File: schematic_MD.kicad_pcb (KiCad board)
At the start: 2 copper layers, 100 x 100 mm, 101 parts, among them J1 XT60, J10 Gate_PWR_Jump, J13 EXPWR_GND, J2 XT60, J3 XT60, J4 CAN_Bus, J5 Rotaly_encoder_1, J6 Rotaly_encoder_2, J7 Z_jumper, J8 Z_jumper, J9 Conn_02x01, Q1 SQJ886EP-T1_GE3, Q2 SQJ886EP-T1_GE3, Q3 SQJ886EP-T1_GE3, Q4 SQJ886EP-T1_GE3, Q5 SQJ886EP-T1_GE3, Q6 SQJ886EP-T1_GE3, Q7 SQJ886EP-T1_GE3, Q8 SQJ886EP-T1_GE3, SW1 SW_MEC_5G, U2 XC6206P332MR-G, U6 STM32F405RGTx, U7 MAX3051, U8 L78M05ABDT-TR

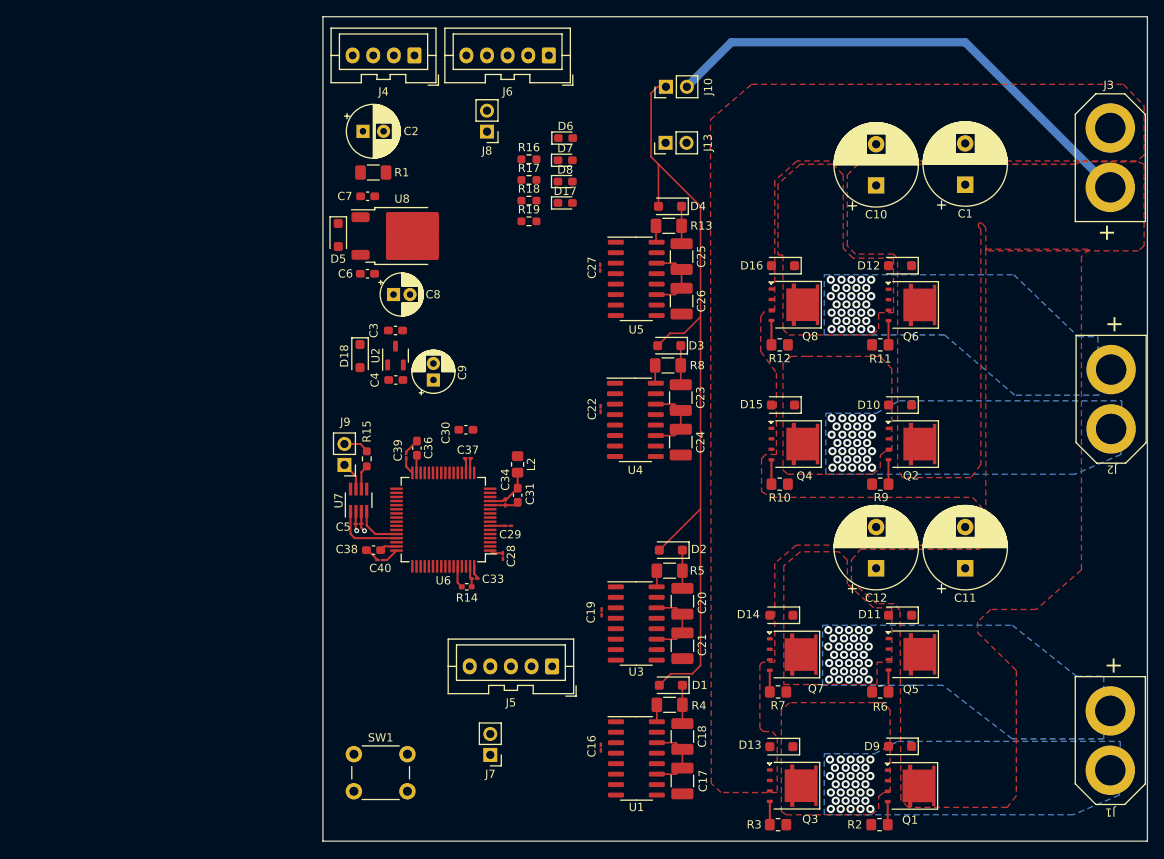
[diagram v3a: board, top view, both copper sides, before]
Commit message: Change gate driver
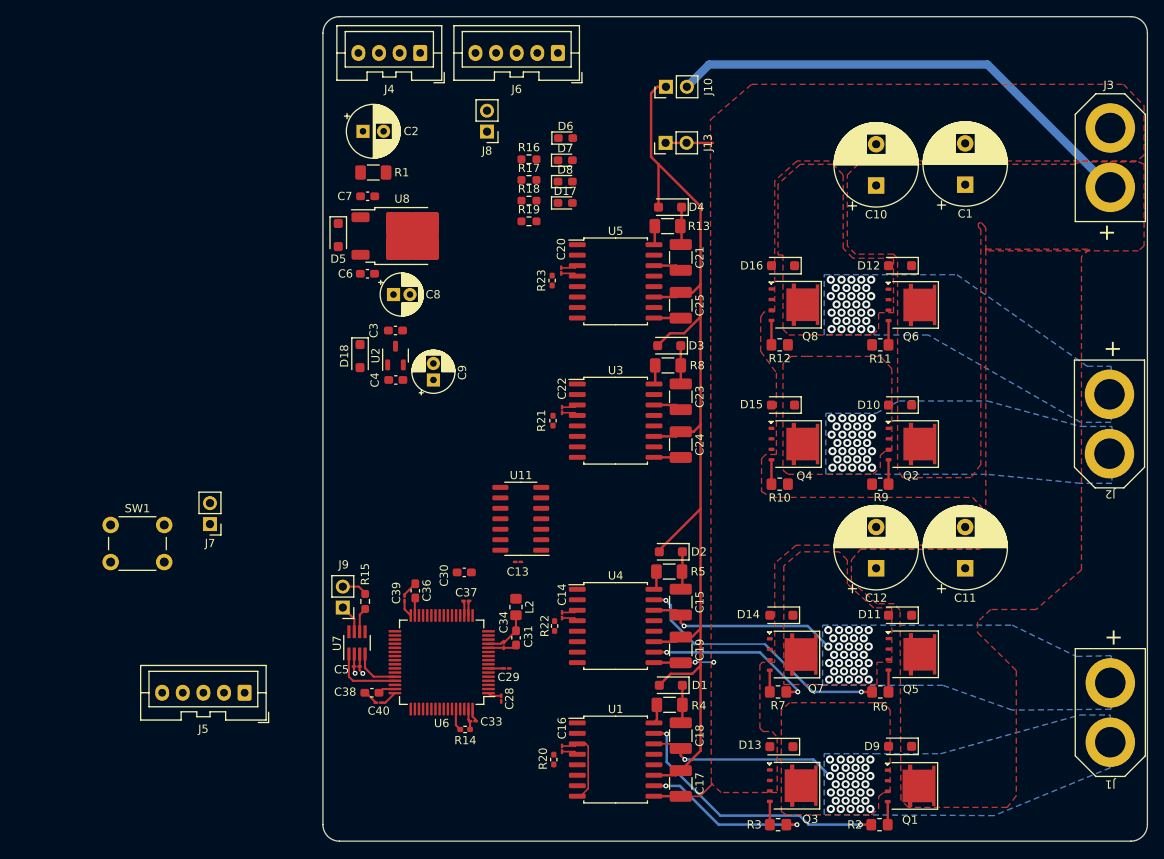
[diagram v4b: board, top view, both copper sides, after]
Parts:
- removed C26: 10u, Capacitor_SMD:C_1210_3225Metric_Pad1.33x2.70mm_HandSolder
- removed C27: 0.1u, Capacitor_SMD:C_01005_0402Metric_Pad0.57x0.30mm_HandSolder
- added C13: 0.1u, Capacitor_SMD:C_01005_0402Metric_Pad0.57x0.30mm_HandSolder, F.Cu at (118.7, 106.1)
- added C14: 0.1u, Capacitor_SMD:C_01005_0402Metric_Pad0.57x0.30mm_HandSolder, F.Cu at (124.0, 112.6)
- added C15: 10u, Capacitor_SMD:C_1210_3225Metric_Pad1.33x2.70mm_HandSolder, F.Cu at (138.4, 111.0)
- added R20: 10k, Resistor_SMD:R_0402_1005Metric_Pad0.72x0.64mm_HandSolder, F.Cu at (123.0, 130.1)
- added R21: 10k, Resistor_SMD:R_0402_1005Metric_Pad0.72x0.64mm_HandSolder, F.Cu at (122.9, 89.0)
- added R22: 10k, Resistor_SMD:R_0402_1005Metric_Pad0.72x0.64mm_HandSolder, F.Cu at (123.1, 113.9)
- added R23: 10k, Resistor_SMD:R_0402_1005Metric_Pad0.72x0.64mm_HandSolder, F.Cu at (122.8, 72.0)
- added U11: 74HC04, Package_SO:SOIC-14_3.9x8.7mm_P1.27mm, F.Cu at (119.0, 100.9)
- C19: value 0.1u -> 10u; footprint Capacitor_SMD:C_01005_0402Metric_Pad0.57x0.30mm_HandSolder -> Capacitor_SMD:C_1210_3225Metric_Pad1.33x2.70mm_HandSolder
- C20: value 10u -> 0.1u; footprint Capacitor_SMD:C_1210_3225Metric_Pad1.33x2.70mm_HandSolder -> Capacitor_SMD:C_01005_0402Metric_Pad0.57x0.30mm_HandSolder
- U1, U3, U4, U5: value ~ -> UCC21520DW; footprint Package_SO:SOIC-16_3.9x9.9mm_P1.27mm -> Package_SO:SOIC-16W_7.5x10.3mm_P1.27mm
- moved C21 47.1 mm to (138.4, 69.2)
- moved J7 44.0 mm to (81.3, 101.5)
- moved C20 42.7 mm to (123.9, 70.8)
- moved SW1 40.5 mm to (69.2, 101.7)
- moved J5 37.4 mm to (85.5, 122.0)
- moved U4 25.1 mm to (130.5, 113.9)
- moved U3 24.7 mm to (130.5, 89.0)
- moved C28 17.3 mm to (116.6, 122.7)
- moved C30 17.3 mm to (112.1, 107.4)
- moved C34 17.3 mm to (116.9, 116.2)
- moved J9 17.3 mm to (97.4, 111.7)
- moved C29 17.3 mm to (117.3, 119.0)
- moved C31 17.3 mm to (118.4, 115.3)
- moved C33 17.3 mm to (113.2, 125.5)
- moved C36 17.3 mm to (106.2, 109.6)
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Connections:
- C17 pad 1: /Driver/H-bridge_left -> Gate_power
- C19 pad 1: +3.3V -> Gate_power
- C19 pad 2: GND1 -> GND2
- C20 pad 1: Net-(D2-K) -> +3.3V
- C20 pad 2: /Driver/H-bridge_right -> GND1
- C21 pad 1: /Driver/H-bridge_right -> Net-(D4-K)
- C21 pad 2: GND2 -> /Driver1/H-bridge_right
- C24 pad 1: /Driver1/H-bridge_left -> Gate_power
- C25 pad 1: Net-(D4-K) -> Gate_power
- C25 pad 2: /Driver1/H-bridge_right -> GND2
- R10 pad 1: Net-(U4-VOB) -> Net-(U3-OUTB)
- R5 pad 1: Net-(U3-VDDA) -> Net-(U4-VDDA)
- R6 pad 1: Net-(U3-VOA) -> Net-(U4-OUTA)
- R7 pad 1: Net-(U3-VOB) -> Net-(U4-OUTB)
- R8 pad 1: Net-(U4-VDDA) -> Net-(U3-VDDA)
- R9 pad 1: Net-(U4-VOA) -> Net-(U3-OUTA)
- U1 pad 11: /Driver/H-bridge_left -> Gate_power
- U1 pad 5: GND1 -> /Driver/EN_left
- U3 pad 1: /Driver/Right_Highside_PWM_IN -> /Driver1/Left_Highside_PWM_IN
- U3 pad 10: Net-(U3-VOB) -> Net-(U3-OUTB)
- U3 pad 11: /Driver/H-bridge_right -> Gate_power
- U3 pad 14: /Driver/H-bridge_right -> /Driver1/H-bridge_left
- U3 pad 15: Net-(U3-VOA) -> Net-(U3-OUTA)
- U3 pad 2: /Driver/Right_Lowside_PWM_IN -> /Driver1/Left_Lowside_PWM_IN
- U3 pad 5: GND1 -> /Driver1/EN_left
- U4 pad 1: /Driver1/Left_Highside_PWM_IN -> /Driver/Right_Highside_PWM_IN
- U4 pad 10: Net-(U4-VOB) -> Net-(U4-OUTB)
- U4 pad 11: /Driver1/H-bridge_left -> Gate_power
- U4 pad 14: /Driver1/H-bridge_left -> /Driver/H-bridge_right
- U4 pad 15: Net-(U4-VOA) -> Net-(U4-OUTA)
- U4 pad 2: /Driver1/Left_Lowside_PWM_IN -> /Driver/Right_Lowside_PWM_IN
- U4 pad 5: GND1 -> /Driver/EN_right
- U5 pad 11: /Driver1/H-bridge_right -> Gate_power
- U5 pad 5: GND1 -> /Driver1/EN_right
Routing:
- net Gate_power: track 98.9 -> 134.9 mm
- net Net-(U1-OUTA): track 0.00 -> 32.9 mm, vias 0 -> 2
- net Net-(U4-OUTA): track 0.00 -> 32.1 mm, vias 0 -> 2
- net GND2: track 0.00 -> 27.3 mm, vias 0 -> 2
- net Net-(U4-OUTB): track 0.00 -> 21.0 mm, vias 0 -> 2
- net Net-(U1-OUTB): track 0.00 -> 20.6 mm, vias 0 -> 2
- net +3.3V: track 11.1 -> 27.3 mm
- net /Driver/H-bridge_right: track 10.9 -> 25.2 mm, vias 32 -> 33
- net /Driver/H-bridge_left: track 10.8 -> 25.1 mm, vias 32 -> 33
- net GND1: track 13.3 -> 21.3 mm
- net /Driver1/H-bridge_left: track 8.96 -> 3.49 mm
- net /Driver1/H-bridge_right: track 8.97 -> 3.49 mm
- net Vdrive: track 60.9 -> 58.7 mm
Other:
- outline, holes or cut-outs redrawn

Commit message: fix design
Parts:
- moved J5 31.4 mm to (109.0, 101.2)
- moved SW1 30.7 mm to (97.2, 89.2)
- moved J7 27.9 mm to (107.6, 92.3)
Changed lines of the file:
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@@
   )
   (footprint "Button_Switch_THT:SW_PUSH_6mm" (layer "F.Cu")
-    (at 69.25 101.65)
+    (at 97.25 89.15)
     (descr "https://www.omron.com/ecb/products/pdf/en-b3f.pdf")
     (tags "tact sw push 6mm")
@@
   )
   (footprint "Connector_PinHeader_2.54mm:PinHeader_1x02_P2.54mm_Vertical" (layer "F.Cu")
-    (at 81.3 101.54 180)
+    (at 107.6 92.34 180)
     (descr "Through hole straight pin header, 1x02, 2.54mm pitch, single row")
     (tags "Through hole pin header THT 1x02 2.54mm single row")
@@
   )
   (footprint "Connector_JST:JST_XA_B05B-XASK-1_1x05_P2.50mm_Vertical" (layer "F.Cu")
-    (at 85.5 122 180)
+    (at 109 101.2 180)
     (descr "JST XA series connector, B05B-XASK-1 (http://www.jst-mfg.com/product/pdf/eng/eXA1.pdf), generated with kicad-footprint-generator")
     (tags "connector JST XA vertical")
@@
     (connect_pads (clearance 0.5))
     (min_thickness 0.25) (filled_areas_thickness no)
-    (fill yes (thermal_gap 0.5) (thermal_bridge_width 0.5))
+    (fill (thermal_gap 0.5) (thermal_bridge_width 0.5))
     (polygon
       (pts
@@
         (xy 190.5 124.7)
         (xy 190.5 131.1)
-        (xy 176.4 136.9)
+        (xy 176.3 136.8)
         (xy 155.8 136.8)
       )

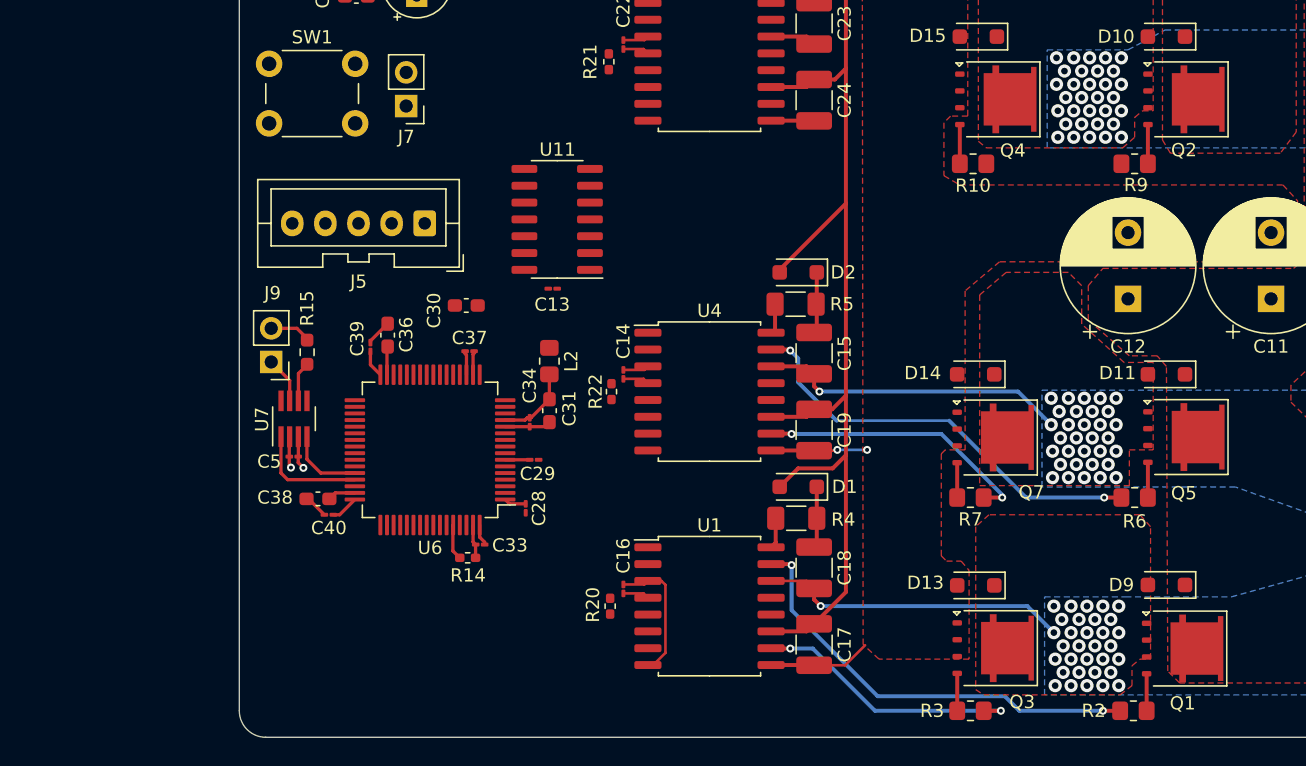
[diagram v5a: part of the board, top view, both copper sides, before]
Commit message: add MOSFET pulldown
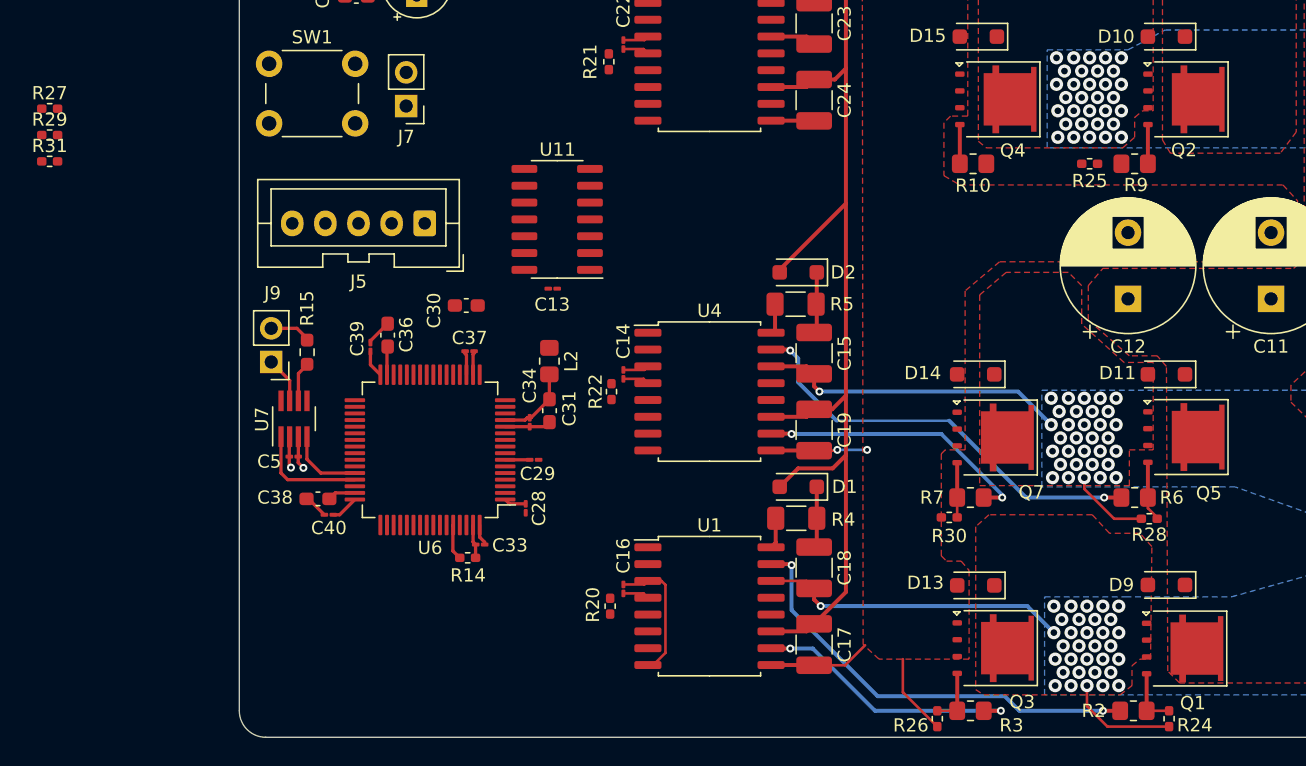
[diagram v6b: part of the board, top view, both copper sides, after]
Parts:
- added R24: 10k, Resistor_SMD:R_0402_1005Metric_Pad0.72x0.64mm_HandSolder, F.Cu at (165.2, 138.6)
- added R25: 10k, Resistor_SMD:R_0402_1005Metric_Pad0.72x0.64mm_HandSolder, F.Cu at (159.2, 96.7)
- added R26: 10k, Resistor_SMD:R_0402_1005Metric_Pad0.72x0.64mm_HandSolder, F.Cu at (147.7, 138.6)
- added R27: 10k, Resistor_SMD:R_0402_1005Metric_Pad0.72x0.64mm_HandSolder, F.Cu at (80.7, 92.5)
- added R28: 10k, Resistor_SMD:R_0402_1005Metric_Pad0.72x0.64mm_HandSolder, F.Cu at (163.7, 123.5)
- added R29: 10k, Resistor_SMD:R_0402_1005Metric_Pad0.72x0.64mm_HandSolder, F.Cu at (80.7, 94.5)
- added R30: 10k, Resistor_SMD:R_0402_1005Metric_Pad0.72x0.64mm_HandSolder, F.Cu at (148.6, 123.4)
- added R31: 10k, Resistor_SMD:R_0402_1005Metric_Pad0.72x0.64mm_HandSolder, F.Cu at (80.7, 96.5)
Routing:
- net /Driver/H-bridge_left: track 25.1 -> 33.5 mm
- net GND2: track 27.3 -> 33.4 mm
- net /Driver/H-bridge_right: track 25.2 -> 31.3 mm
- net Net-(Q5-G): track 2.96 -> 4.89 mm
- net Net-(Q3-G): track 2.76 -> 4.27 mm
- net Net-(Q7-G): track 2.64 -> 4.14 mm
- net Net-(Q1-G): track 2.63 -> 4.09 mm

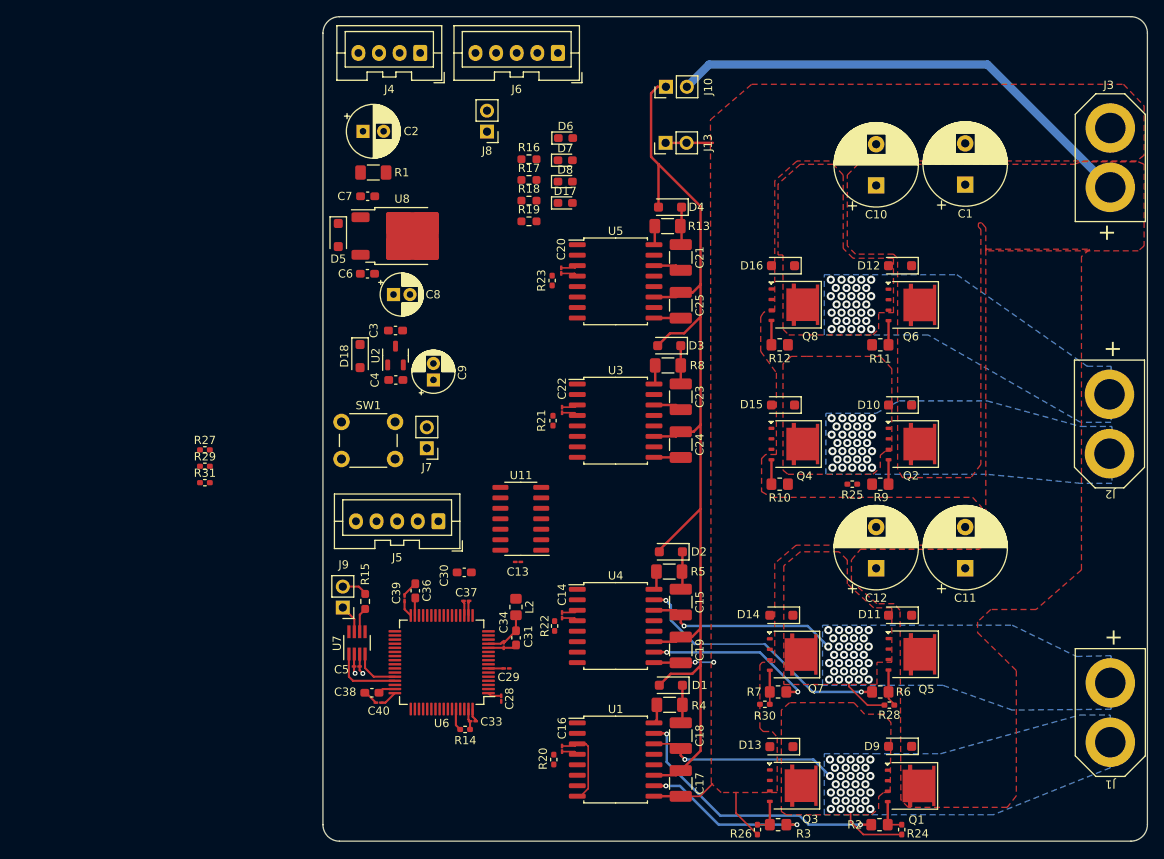
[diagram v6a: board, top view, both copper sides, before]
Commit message: fix powerline
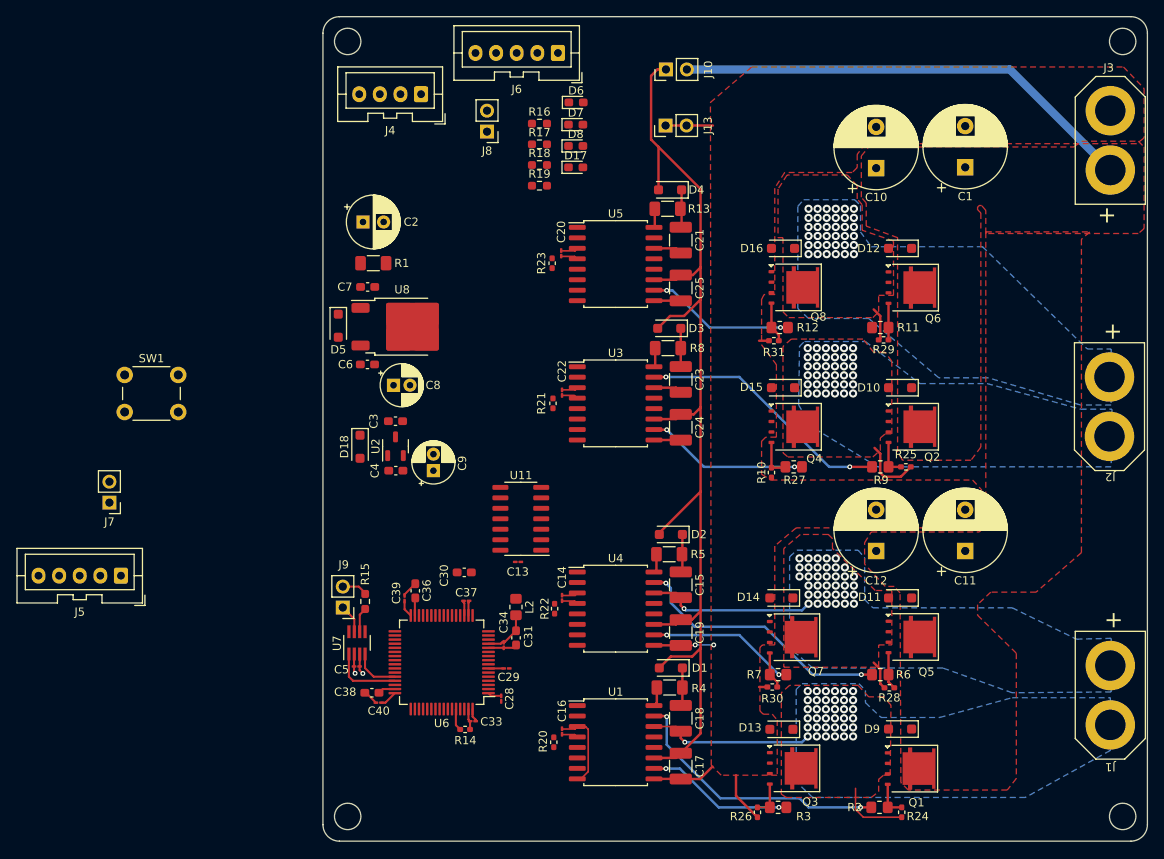
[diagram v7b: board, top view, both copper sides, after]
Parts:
- moved R29 83.7 mm to (163.0, 79.2), turned to 180 degrees
- moved R31 71.1 mm to (149.7, 79.3), turned to 180 degrees
- moved R27 68.8 mm to (149.4, 95.3), turned to -90 degrees
- moved J5 39.1 mm to (70.5, 107.8)
- moved J7 39.1 mm to (69.1, 98.9)
- moved SW1 26.9 mm to (71.0, 83.5)
- moved C2 11.0 mm to (99.9, 64.9)
- moved R1 11.0 mm to (101.1, 69.9)
- moved C3 11.0 mm to (103.8, 89.1)
- moved C4 11.0 mm to (103.8, 95.1)
- moved C6 11.0 mm to (100.4, 82.2)
- moved C7 11.0 mm to (100.4, 72.8)
- moved C8 11.0 mm to (103.6, 84.7)
- moved C9 11.0 mm to (108.4, 95.1)
- moved D18 11.0 mm to (99.5, 92.2)
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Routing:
- net Net-(U3-OUTA): track 0.00 -> 31.0 mm, vias 0 -> 2
- net Net-(U3-OUTB): track 0.00 -> 19.8 mm, vias 0 -> 2
- net Net-(U5-OUTB): track 0.00 -> 18.1 mm, vias 0 -> 2
- net /Driver1/H-bridge_left: track 3.49 -> 11.2 mm, vias 32 -> 36
- net /Driver/H-bridge_right: track 31.3 -> 25.8 mm, vias 33 -> 37
- net /Driver1/H-bridge_right: track 3.49 -> 7.60 mm, vias 32 -> 36
- net /Driver/H-bridge_left: track 33.5 -> 30.4 mm, vias 33 -> 37
- net Net-(U4-OUTB): track 21.0 -> 18.0 mm
- net Net-(U1-OUTB): track 20.6 -> 18.0 mm
- net Vdrive: track 58.7 -> 56.4 mm
- net Net-(Q4-G): track 2.64 -> 4.84 mm
- net GND2: track 33.4 -> 35.5 mm
- net Net-(Q8-G): track 2.76 -> 4.73 mm
- net Net-(Q2-G): track 2.96 -> 4.47 mm
- net Net-(Q6-G): track 2.74 -> 4.24 mm
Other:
- outline, holes or cut-outs redrawn
